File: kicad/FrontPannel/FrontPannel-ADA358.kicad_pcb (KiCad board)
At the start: 2 copper layers, 198 x 58 mm, 18 parts

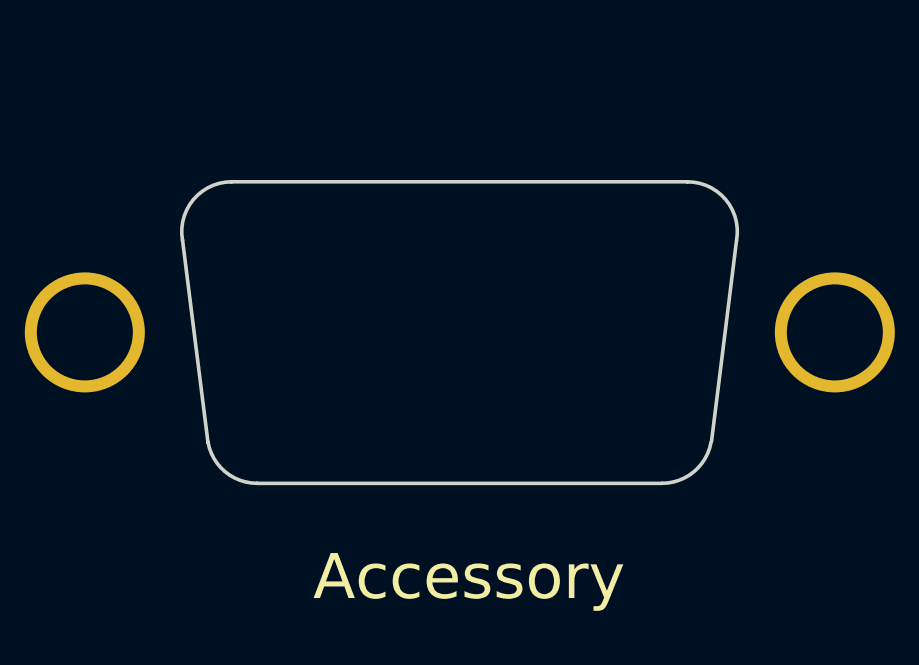
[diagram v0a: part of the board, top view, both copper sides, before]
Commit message: fix board outline for front panel and mainboad (#139)
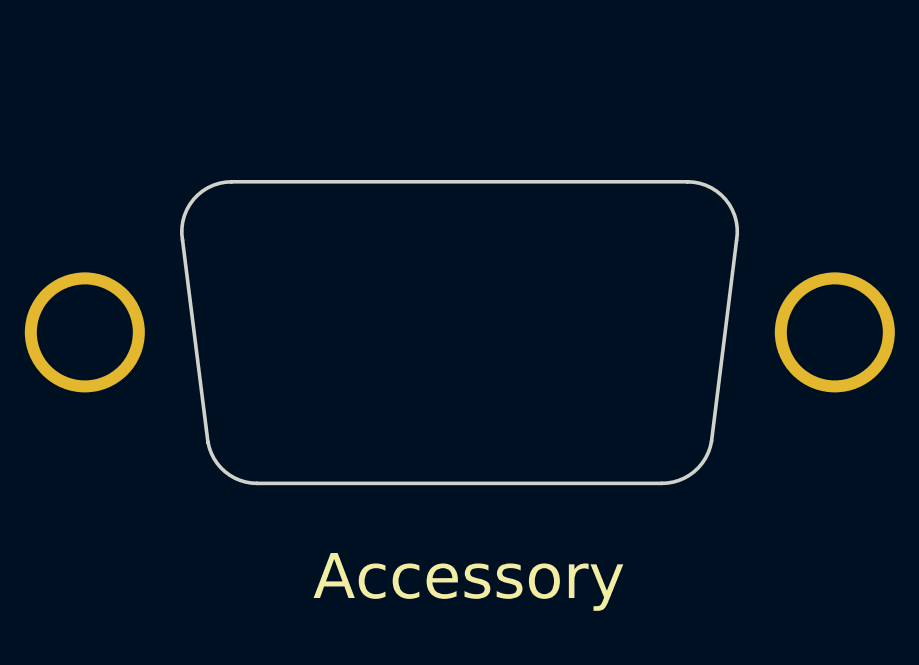
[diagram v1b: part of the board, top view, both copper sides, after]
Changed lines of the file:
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@@
     (fp_line (start -2.1971 0.9525) (end 11.2903 0.9525) (layer "Edge.Cuts") (width 0.12))
     (fp_line (start -3.05 -9.1) (end 12.15 -9.1) (layer "Edge.Cuts") (width 0.12))
-    (fp_line (start 13.78204 -7.13232) (end 12.95 -0.45) (layer "Edge.Cuts") (width 0.12))
-    (fp_arc (start -2.2 0.95) (mid -3.267028 0.561634) (end -3.834781 -0.421744) (layer "Edge.Cuts") (width 0.12))
-    (fp_arc (start -4.684781 -7.151744) (mid -4.321634 -8.507028) (end -3.05 -9.1) (layer "Edge.Cuts") (width 0.12))
-    (fp_arc (start 12.934781 -0.421744) (mid 12.367028 0.561634) (end 11.3 0.95) (layer "Edge.Cuts") (width 0.12))
-    (fp_arc (start 12.15 -9.1) (mid 13.421634 -8.507027) (end 13.784781 -7.151744) (layer "Edge.Cuts") (width 0.12))
+    (fp_line (start 13.784781 -7.151744) (end 12.95 -0.45) (layer "Edge.Cuts") (width 0.12))
+    (fp_arc (start -2.1971 0.9525) (mid -3.266023 0.563401) (end -3.834781 -0.421744) (layer "Edge.Cuts") (width 0.12))
+    (fp_arc (start -4.68376 -7.15772) (mid -4.319017 -8.509177) (end -3.05 -9.1) (layer "Edge.Cuts") (width 0.12))
+    (fp_arc (start 12.95 -0.45) (mid 12.378368 0.556822) (end 11.2903 0.9525) (layer "Edge.Cuts") (width 0.12))
+    (fp_arc (start 12.15 -9.1) (mid 13.421632 -8.507026) (end 13.784781 -7.151744) (layer "Edge.Cuts") (width 0.12))
     (fp_line (start 19.985 -9.33) (end 19.985 1.17) (layer "F.Fab") (width 0.1))
     (fp_line (start -9.865 -10.33) (end 18.985 -10.33) (layer "F.Fab") (width 0.1))
@@
     (fp_arc (start -9.865 2.17) (mid -10.572107 1.877107) (end -10.865 1.17) (layer "F.Fab") (width 0.1))
     (fp_arc (start 19.985 1.17) (mid 19.692107 1.877107) (end 18.985 2.17) (layer "F.Fab") (width 0.1))
-    (pad "0" thru_hole circle locked (at 17.06 -4.08) (size 4 4) (drill 3.2) (layers *.Cu *.Mask)
+    (pad "0" thru_hole circle (at 17.06 -4.08) (size 4 4) (drill 3.2) (layers *.Cu *.Mask)
       (net 1 "GND"))
-    (pad "0" thru_hole circle locked (at -7.94 -4.08) (size 4 4) (drill 3.2) (layers *.Cu *.Mask)
+    (pad "0" thru_hole circle (at -7.94 -4.08) (size 4 4) (drill 3.2) (layers *.Cu *.Mask)
       (net 1 "GND"))
     (model "${KISYS3DMOD}/Connector_Dsub.3dshapes/DSUB-9_Female_Vertical_P2.77x2.84mm_MountingHoles.wrl"
